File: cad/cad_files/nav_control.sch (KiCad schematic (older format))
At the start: 6 parts

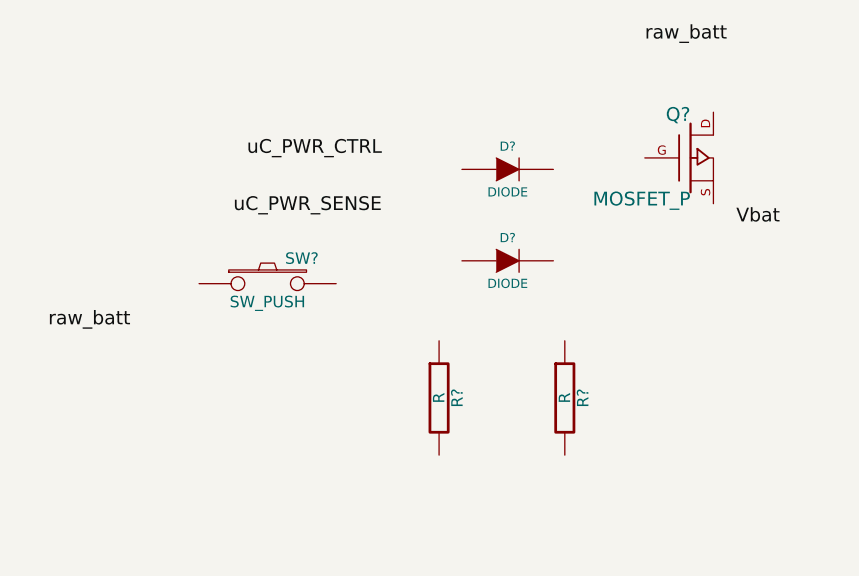
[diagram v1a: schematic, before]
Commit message: adding wires for nav_control soft power
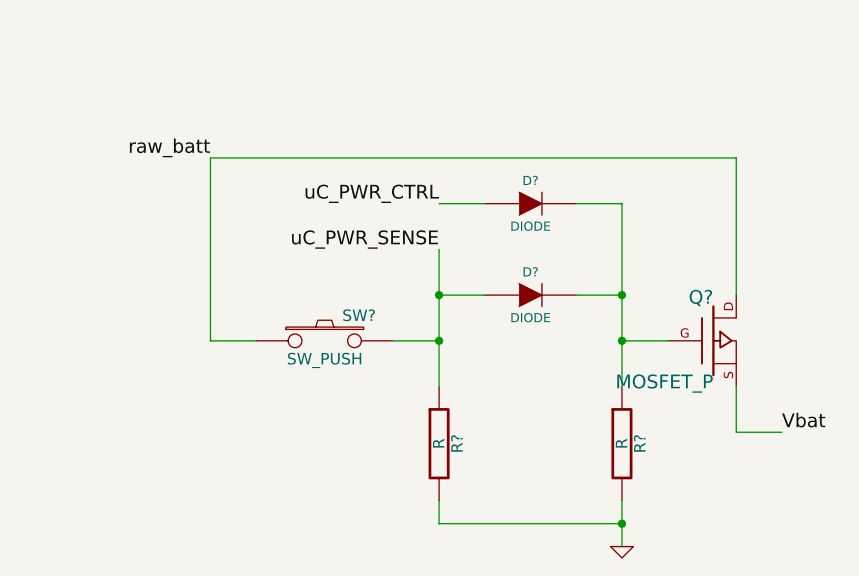
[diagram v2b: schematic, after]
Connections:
- net Vbat: now also Q?.S
- net raw_batt: now also Q?.D, SW?.1
- net uC_PWR_CTRL: now also D?.1 (A)
- net uC_PWR_SENSE: now also D?.1 (A), R?.1, SW?.2
- net GND: now reaches R?.2
- net GND: now also R?.2
- net at R?.1: now also D?.2 (K), D?.2 (K), Q?.G
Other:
- moved on the sheet: D?, Q?, R?, SW?
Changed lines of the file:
@@
-EESchema Schematic File Version 2  date Thu 24 Jul 2014 11:01:35 PM HST
+EESchema Schematic File Version 2  date Fri 01 Aug 2014 11:18:16 AM HST
 LIBS:local_parts
 LIBS:power
@@
 Sheet 3 5
 Title ""
-Date "25 jul 2014"
+Date "1 aug 2014"
 Rev ""
 Comp ""
@@
 Comment4 ""
 $EndDescr
-Text Label 6650 1950 2    60   ~ 0
+Connection ~ 8800 2800
+Wire Wire Line
+	8800 2800 8000 2800
+Wire Wire Line
+	8000 2800 8000 2700
+Wire Wire Line
+	9300 1800 9300 1200
+Wire Wire Line
+	9300 1200 7000 1200
+Wire Wire Line
+	9300 2200 9300 2400
+Wire Wire Line
+	9300 2400 9500 2400
+Connection ~ 8800 1800
+Wire Wire Line
+	8800 2200 8800 1400
+Wire Wire Line
+	8800 1400 8600 1400
+Wire Wire Line
+	8800 1800 8600 1800
+Connection ~ 8000 2000
+Wire Wire Line
+	7800 2000 8000 2000
+Wire Wire Line
+	8000 1600 8000 2200
+Wire Wire Line
+	8200 1800 8000 1800
+Connection ~ 8000 1800
+Wire Wire Line
+	8000 1400 8200 1400
+Wire Wire Line
+	9000 2000 8800 2000
+Connection ~ 8800 2000
+Wire Wire Line
+	7000 1200 7000 2000
+Wire Wire Line
+	7000 2000 7200 2000
+Wire Wire Line
+	8800 2700 8800 2900
+$Comp
+L GND #PWR?
+U 1 1 53DB8078
+P 8800 2900
+F 0 "#PWR?" H 8800 2900 30  0001 C CNN
+F 1 "GND" H 8800 2830 30  0001 C CNN
+	1    8800 2900
+	1    0    0    -1
+$EndComp
+Text Label 7000 1200 2    60   ~ 0
 raw_batt
-Text Label 7750 1450 2    60   ~ 0
+Text Label 8000 1600 2    60   ~ 0
 uC_PWR_SENSE
-Text Label 7750 1200 2    60   ~ 0
+Text Label 8000 1400 2    60   ~ 0
 uC_PWR_CTRL
-Text Label 8900 700  0    60   ~ 0
-raw_batt
-Text Label 9300 1500 0    60   ~ 0
+Text Label 9500 2400 0    60   ~ 0
 Vbat
 $Comp
 L MOSFET_P Q?
 U 1 1 53D1B1AA
-P 9100 1200
-F 0 "Q?" H 9100 1390 60  0000 R CNN
-F 1 "MOSFET_P" H 9100 1020 60  0000 R CNN
-	1    9100 1200
+P 9200 2000
+F 0 "Q?" H 9200 2190 60  0000 R CNN
+F 1 "MOSFET_P" H 9200 1820 60  0000 R CNN
+	1    9200 2000
 	1    0    0    -1
 $EndComp
@@
 L DIODE D?
 U 1 1 53D1B1A5
-P 8300 1250
-F 0 "D?" H 8300 1350 40  0000 C CNN
-F 1 "DIODE" H 8300 1150 40  0000 C CNN
-	1    8300 1250
+P 8400 1400
+F 0 "D?" H 8400 1500 40  0000 C CNN
+F 1 "DIODE" H 8400 1300 40  0000 C CNN
+	1    8400 1400
 	1    0    0    -1
 $EndComp
@@
 L DIODE D?
 U 1 1 53D1B19F
-P 8300 1650
-F 0 "D?" H 8300 1750 40  0000 C CNN
-F 1 "DIODE" H 8300 1550 40  0000 C CNN
-	1    8300 1650
+P 8400 1800
+F 0 "D?" H 8400 1900 40  0000 C CNN
+F 1 "DIODE" H 8400 1700 40  0000 C CNN
+	1    8400 1800
 	1    0    0    -1
 $EndComp
@@
 L R R?
 U 1 1 53D1B197
-P 8550 2250
-F 0 "R?" V 8630 2250 50  0000 C CNN
-F 1 "R" V 8550 2250 50  0000 C CNN
-	1    8550 2250
+P 8800 2450
+F 0 "R?" V 8880 2450 50  0000 C CNN
+F 1 "R" V 8800 2450 50  0000 C CNN
+	1    8800 2450
 	1    0    0    -1
 $EndComp
@@
 L R R?
 U 1 1 53D1B192
-P 8000 2250
-F 0 "R?" V 8080 2250 50  0000 C CNN
-F 1 "R" V 8000 2250 50  0000 C CNN
-	1    8000 2250
+P 8000 2450
+F 0 "R?" V 8080 2450 50  0000 C CNN
+F 1 "R" V 8000 2450 50  0000 C CNN
+	1    8000 2450
 	1    0    0    -1
 $EndComp
@@
 L SW_PUSH SW?
 U 1 1 53D1B188
-P 7250 1750
-F 0 "SW?" H 7400 1860 50  0000 C CNN
-F 1 "SW_PUSH" H 7250 1670 50  0000 C CNN
-	1    7250 1750
+P 7500 2000
+F 0 "SW?" H 7650 2110 50  0000 C CNN
+F 1 "SW_PUSH" H 7500 1920 50  0000 C CNN
+	1    7500 2000
 	1    0    0    -1
 $EndComp

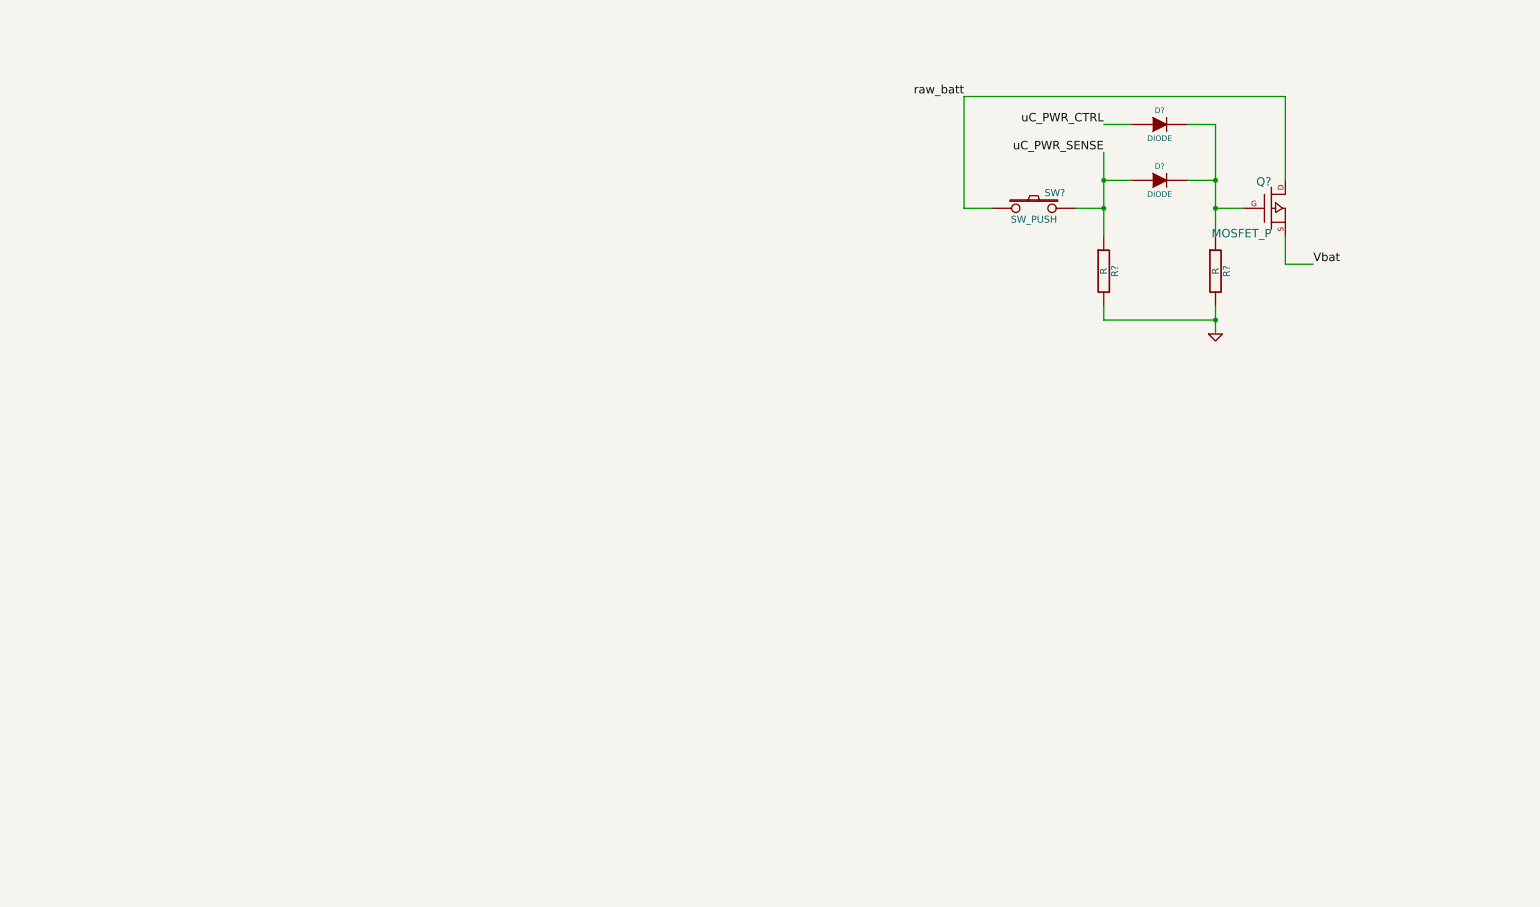
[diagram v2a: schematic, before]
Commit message: Updating control plan
Add notes for signals/pins
Add power supply footprint (boost vbat to 3.3 or 5 V for microcontroller)
Add bypass for power supply switching
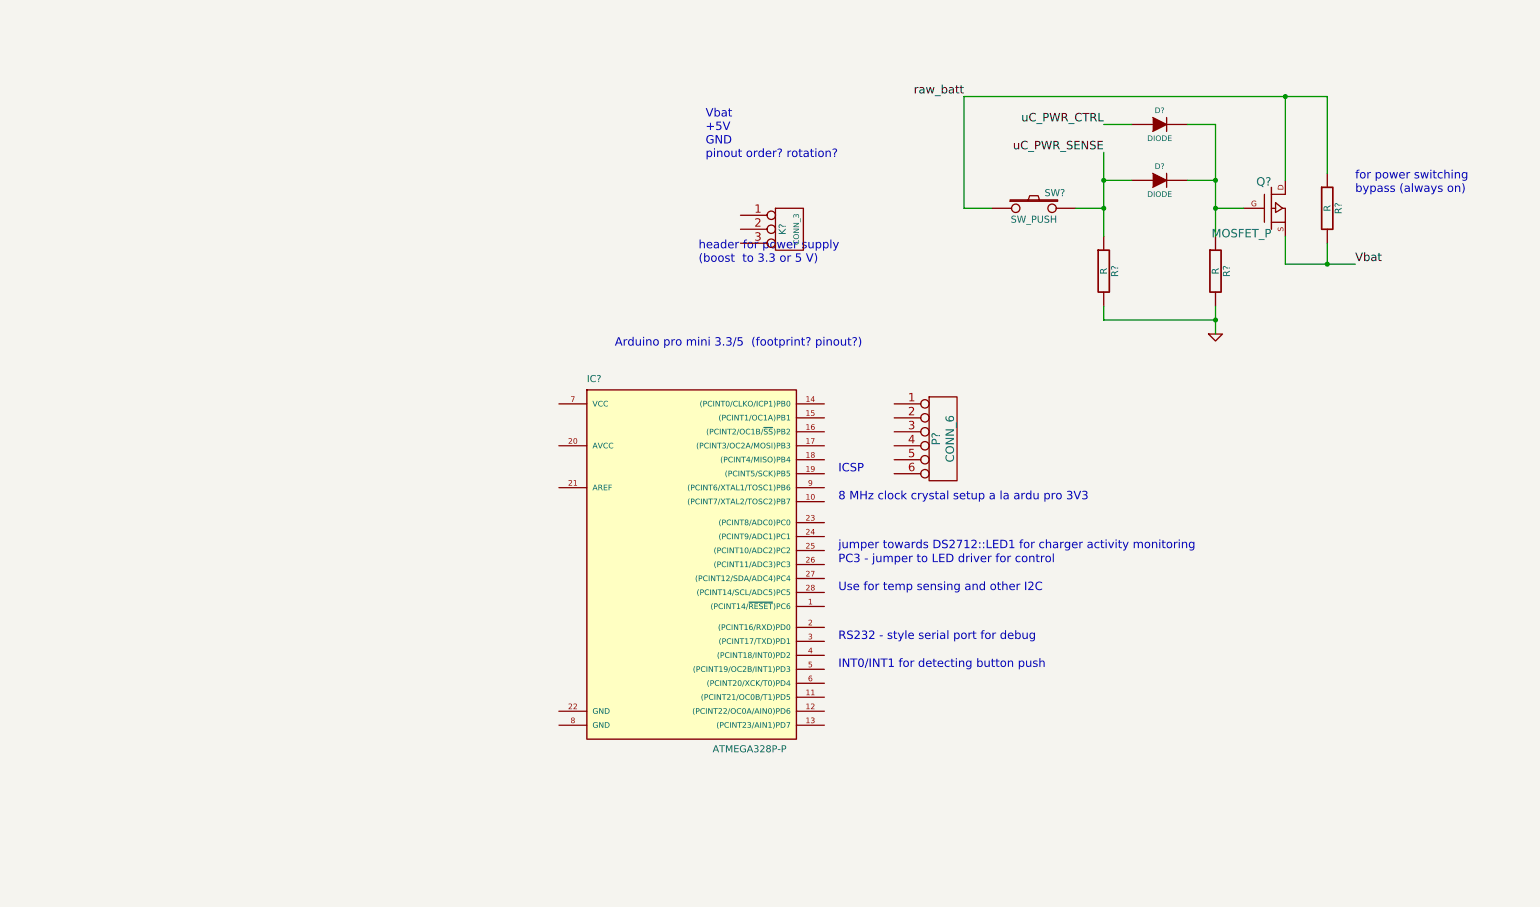
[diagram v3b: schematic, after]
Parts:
- added IC?: ATMEGA328P-P, DIL28, symbol ATMEGA328P-P
- added K?: CONN_3, symbol CONN_3
- added P?: CONN_6, symbol CONN_6
- added R?: R, symbol R
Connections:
- net Vbat: now also R?.2
- net raw_batt: now also R?.1
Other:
- note added: "8 MHz clock crystal setup a la ardu pro 3V3"
- note added: "Arduino pro mini 3.3/5 (footprint? pinout?)"
- note added: "ICSP"
- note added: "INT0/INT1 for detecting button push"
- note added: "PC3 - jumper to LED driver for control"
- note added: "RS232 - style serial port for debug"
- note added: "Use for temp sensing and other I2C"
- note added: "Vbat\n+5V\nGND\npinout order? rotation?"
- note added: "for power switching \nbypass (always on)"
- note added: "header for power supply \n(boost to 3.3 or 5 V)"
- note added: "jumper towards DS2712::LED1 for charger activity monitoring"
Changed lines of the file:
@@
-EESchema Schematic File Version 2  date Fri 01 Aug 2014 11:18:16 AM HST
+EESchema Schematic File Version 2  date Mon 01 Dec 2014 02:47:20 AM HST
 LIBS:local_parts
 LIBS:power
@@
 Sheet 3 5
 Title ""
-Date "1 aug 2014"
+Date "1 dec 2014"
 Rev ""
 Comp ""
@@
 Comment4 ""
 $EndDescr
+Text Notes 4500 3000 0    60   ~ 0
+Arduino pro mini 3.3/5  (footprint? pinout?)
+Text Notes 5150 1650 0    60   ~ 0
+Vbat\n+5V\nGND\npinout order? rotation?
+Text Notes 9800 1900 0    60   ~ 0
+for power switching \nbypass (always on)
+Connection ~ 9300 1200
+Wire Wire Line
+	9600 1200 7000 1200
+Wire Wire Line
+	9600 1200 9600 1750
 Connection ~ 8800 2800
 Wire Wire Line
@@
 	8000 2800 8000 2700
 Wire Wire Line
-	9300 1800 9300 1200
-Wire Wire Line
-	9300 1200 7000 1200
+	9300 1200 9300 1800
 Wire Wire Line
 	9300 2200 9300 2400
 Wire Wire Line
-	9300 2400 9500 2400
+	9300 2400 9800 2400
 Connection ~ 8800 1800
 Wire Wire Line
@@
 	8800 1400 8600 1400
 Wire Wire Line
-	8800 1800 8600 1800
+	8600 1800 8800 1800
 Connection ~ 8000 2000
 Wire Wire Line
 	7800 2000 8000 2000
 Wire Wire Line
-	8000 1600 8000 2200
+	8000 2200 8000 1600
 Wire Wire Line
-	8200 1800 8000 1800
+	8000 1800 8200 1800
 Connection ~ 8000 1800
 Wire Wire Line
 	8000 1400 8200 1400
 Wire Wire Line
-	9000 2000 8800 2000
+	8800 2000 9000 2000
 Connection ~ 8800 2000
 Wire Wire Line
@@
 	7000 2000 7200 2000
 Wire Wire Line
-	8800 2700 8800 2900
+	8800 2900 8800 2700
+Wire Wire Line
+	9600 2250 9600 2400
+Connection ~ 9600 2400
+$Comp
+L R R?
+U 1 1 547C6270
+P 9600 2000
+F 0 "R?" V 9680 2000 50  0000 C CNN
+F 1 "R" V 9600 2000 50  0000 C CNN
+	1    9600 2000
+	1    0    0    -1
+$EndComp
+Text Notes 5100 2400 0    60   ~ 0
+header for power supply \n(boost  to 3.3 or 5 V)
+$Comp
+L CONN_3 K?
+U 1 1 546DDB52
+P 5750 2150
+F 0 "K?" V 5700 2150 50  0000 C CNN
+F 1 "CONN_3" V 5800 2150 40  0000 C CNN
+	1    5750 2150
+	1    0    0    -1
+$EndComp
+Text Notes 6100 4450 0    60   ~ 0
+jumper towards DS2712::LED1 for charger activity monitoring
+Text Notes 6100 4550 0    60   ~ 0
+PC3 - jumper to LED driver for control
+Text Notes 6100 4750 0    60   ~ 0
+Use for temp sensing and other I2C
+Text Notes 6100 5300 0    60   ~ 0
+INT0/INT1 for detecting button push
+Text Notes 6100 5100 0    60   ~ 0
+RS232 - style serial port for debug
+Text Notes 6100 3900 0    60   ~ 0
+ICSP
+Text Notes 6100 4100 0    60   ~ 0
+8 MHz clock crystal setup a la ardu pro 3V3
+$Comp
+L CONN_6 P?
+U 1 1 53DE4465
+P 6850 3650
+F 0 "P?" V 6800 3650 60  0000 C CNN
+F 1 "CONN_6" V 6900 3650 60  0000 C CNN
+	1    6850 3650
+	1    0    0    -1
+$EndComp
+$Comp
+L ATMEGA328P-P IC?
+U 1 1 53DE42CE
+P 5000 4500
+F 0 "IC?" H 4300 5750 50  0000 L BNN
+F 1 "ATMEGA328P-P" H 5200 3100 50  0000 L BNN
+F 2 "DIL28" H 4400 3150 50  0001 C CNN
+	1    5000 4500
+	1    0    0    -1
+$EndComp
 $Comp
 L GND #PWR?
@@
 Text Label 8000 1400 2    60   ~ 0
 uC_PWR_CTRL
-Text Label 9500 2400 0    60   ~ 0
+Text Label 9800 2400 0    60   ~ 0
 Vbat
 $Comp
